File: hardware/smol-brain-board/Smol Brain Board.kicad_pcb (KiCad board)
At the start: 2 copper layers, 44.8 x 52.6 mm, 66 parts, among them J1 USB4085-GF-A, J12 Jumper 2Way Vert Solderable, J3 CAN_DBG, J6 Smol_Brain_Board, J7 PROGRAM, J8 Jumper 2Way Vert Solderable, J9 Jumper 2Way Vert Solderable, U1 ESP32-S3-WROOM-1-N8, U3 SN65HVD231D

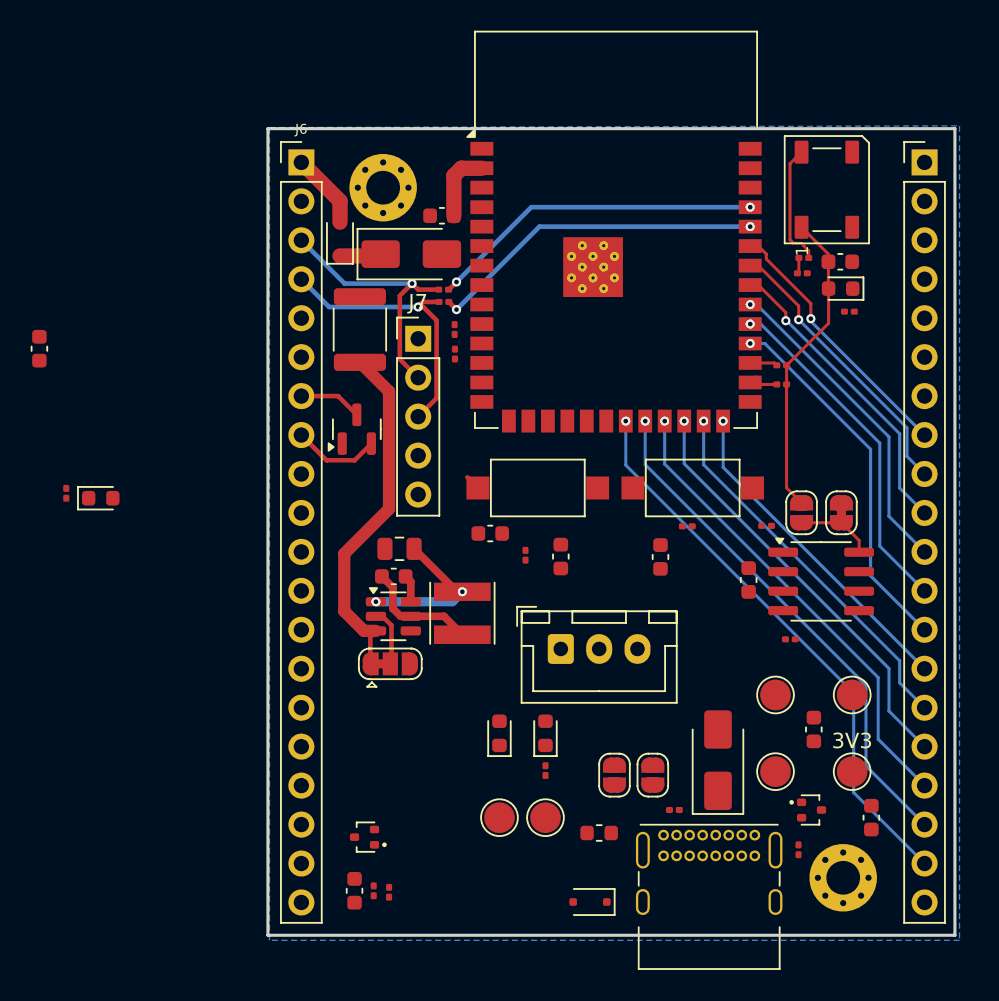
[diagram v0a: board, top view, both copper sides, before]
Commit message: Impedence matching USB data
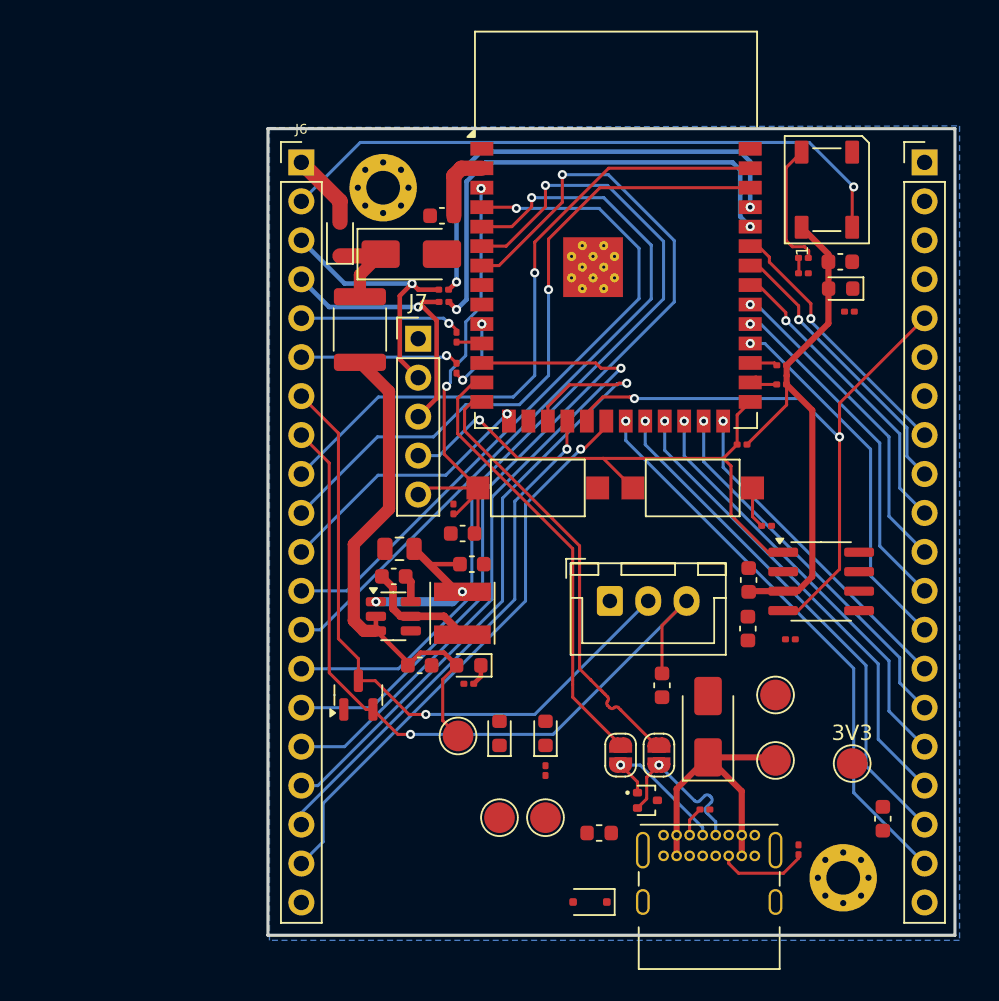
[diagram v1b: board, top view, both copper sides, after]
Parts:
- removed C12: Capacitor 100n 50V 0603, Capacitor_SMD:C_0603_1608Metric
- removed D7: RB558WMTL, Package_TO_SOT_SMD:SOT-416
- removed J12: Jumper 2Way Vert Solderable, Jumper:SolderJumper-2_P1.3mm_Open_RoundedPad1.0x1.5mm
- removed JP1: SolderJumper_2_Bridged, Jumper:SolderJumper-2_P1.3mm_Bridged_RoundedPad1.0x1.5mm
- removed JP3: SolderJumper_3_Bridged12, Jumper:SolderJumper-3_P1.3mm_Bridged12_RoundedPad1.0x1.5mm
- removed R10, R11: Resistor 10k 0603, Resistor_SMD:R_0201_0603Metric
- moved C4 32.3 mm to (135.9, 113.8), turned to 0 degrees
- moved R9 29.0 mm to (139.1, 115.0), turned to 180 degrees
- moved VIN_IND1 26.4 mm to (139.1, 113.8), turned to 180 degrees
- moved C6 24.8 mm to (139.3, 107.2), turned to 0 degrees
- moved VCC1 20.8 mm to (138.4, 118.4)
- moved D3 17.3 mm to (131.9, 115.7)
- moved D6 10.7 mm to (150.8, 122.6)
- moved C11 10.7 mm to (151.7, 115.1), turned to -90 degrees
- moved C8 7.37 mm to (157.3, 111.4)
- moved VBUS1 6.58 mm to (159.1, 120.0)
- moved R19 6.42 mm to (156.9, 99.4)
- moved R6 5.59 mm to (138.1, 103.6), turned to -90 degrees
- moved J3 4.48 mm to (148.3, 109.6)
- moved D2 2.28 mm to (154.7, 117.8)
- moved R4 1.99 mm to (154.5, 123.2), turned to 0 degrees
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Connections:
- C4 pad 1: Net-(JP3-A) -> Net-(VIN_IND1-A)
- F1 pad 1: Net-(JP3-A) -> Net-(VIN_IND1-A)
- F2 pad 2: Net-(JP3-A) -> Net-(VIN_IND1-A)
- U3 pad 8: Net-(J12-A) -> GND
- VCC1 pad 1: Net-(JP3-A) -> Net-(VIN_IND1-A)
- VIN_IND1 pad 2: Net-(JP3-A) -> Net-(VIN_IND1-A)
- VR1 pad 2: Net-(JP3-C) -> Net-(VIN_IND1-A)
- VR1 pad 3: Net-(JP3-A) -> Net-(VIN_IND1-A)
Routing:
- net /A7: track 0.00 -> 61.0 mm, vias 0 -> 1
- net /A6: track 0.00 -> 57.2 mm, vias 0 -> 1
- net /A5: track 0.00 -> 48.7 mm, vias 0 -> 1
- net /A4: track 0.00 -> 44.6 mm, vias 0 -> 1
- net /CAN_L: track 5.70 -> 50.2 mm, vias 0 -> 1
- net /A8: track 0.00 -> 44.2 mm, vias 0 -> 1
- net /A2: track 0.00 -> 43.3 mm, vias 0 -> 1
- net /A9: track 0.00 -> 42.7 mm, vias 0 -> 1
- net /A1: track 0.00 -> 42.6 mm, vias 0 -> 1
- net /CAN_RX: track 0.00 -> 42.1 mm, vias 0 -> 2
- net /LED_DOUT: track 0.00 -> 41.5 mm, vias 0 -> 1
- net /CAN_H: track 4.13 -> 43.0 mm, vias 0 -> 1
- net /CAN_TX: track 0.00 -> 37.3 mm, vias 0 -> 1
- net /IO12: track 0.00 -> 37.2 mm, vias 0 -> 1
- net Net-(VIN_IND1-A): track 0.00 -> 33.9 mm
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
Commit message: Rough route and via stitching, needs trace width correction
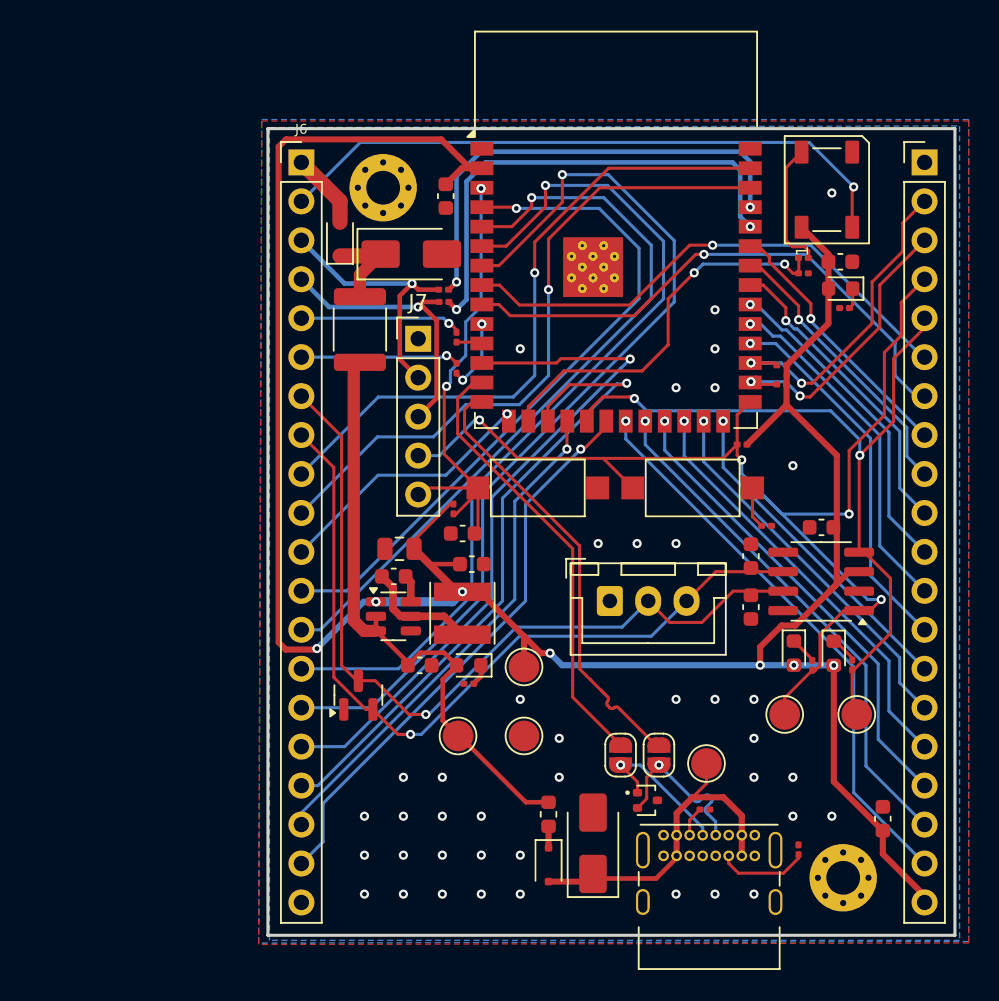
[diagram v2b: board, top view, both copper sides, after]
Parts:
- moved CAN_RX1 24.3 mm to (164.4, 117.0)
- moved 3V3 22.3 mm to (142.7, 113.9)
- moved R14 21.1 mm to (164.1, 113.8)
- moved CTX1 19.9 mm to (160.3, 113.0), turned to -90 degrees
- moved CRX1 19.5 mm to (162.9, 113.0), turned to -90 degrees
- moved CAN_TX1 17.0 mm to (159.7, 117.0)
- moved GND1 16.6 mm to (142.7, 118.4)
- moved D2 10.7 mm to (147.2, 125.4)
- moved C11 10.2 mm to (157.5, 106.7), turned to 90 degrees
- moved C7 5.86 mm to (162.1, 104.8), turned to 180 degrees
- moved VBUS1 4.50 mm to (154.6, 120.2)
- moved D4 3.63 mm to (144.3, 126.8), turned to -90 degrees
- moved F2 3.52 mm to (144.3, 123.5), turned to 90 degrees
- moved R12 2.22 mm to (161.5, 113.8), turned to 90 degrees
- moved C8 1.41 mm to (157.5, 110.0)
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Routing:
- net 3V3: track 54.1 -> 161.8 mm, vias 2 -> 7
- net /CAN_TX: track 37.3 -> 78.5 mm, vias 1 -> 4
- net /IO16: track 0.00 -> 36.6 mm, vias 0 -> 1
- net /IO15: track 0.00 -> 34.0 mm, vias 0 -> 1
- net /uC_LED: track 1.04 -> 25.4 mm, vias 0 -> 2
- net /I2C_SCK: track 1.80 -> 21.2 mm, vias 0 -> 2
- net /I2C_SDA: track 2.31 -> 19.9 mm, vias 0 -> 2
- net /CAN_H: track 43.0 -> 53.3 mm
- net /CAN_RX: track 42.1 -> 51.1 mm
- net Net-(VIN_IND1-A): track 33.9 -> 40.0 mm
- net VBUS: track 19.1 -> 22.5 mm
- net Net-(CRX1-K): track 0.00 -> 1.80 mm
- net Net-(CTX1-K): track 0.00 -> 1.76 mm
- net /CAN_L: track 50.2 -> 51.9 mm
- net /A8: track 44.2 -> 45.6 mm
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- added copper zone on F.Cu, net GND

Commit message: Routing complete, DRC passing, inspection required
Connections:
- J6 pad 41: GND -> (no net)
- J6 pad 42: GND -> (no net)
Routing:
- net GND: vias 40 -> 75

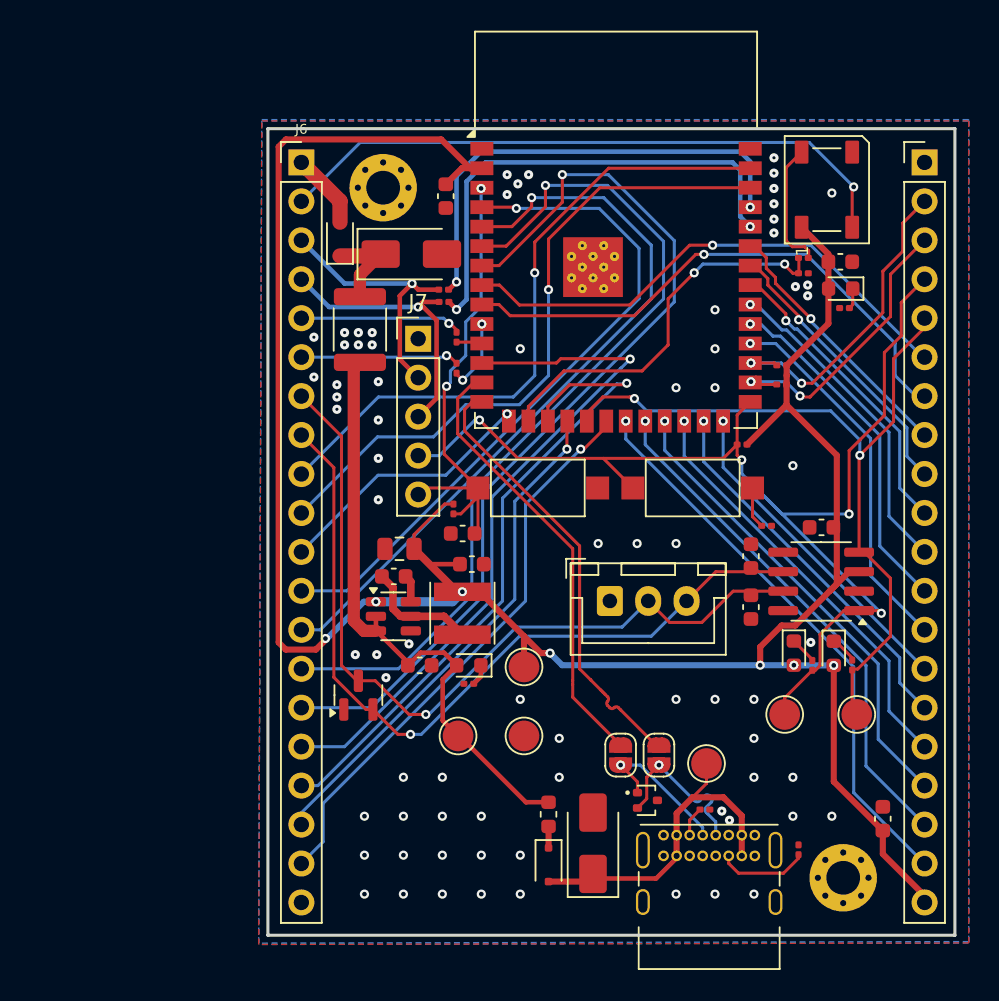
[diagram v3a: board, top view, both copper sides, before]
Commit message: Fixed impedance matching for USB and decoupling cap placement
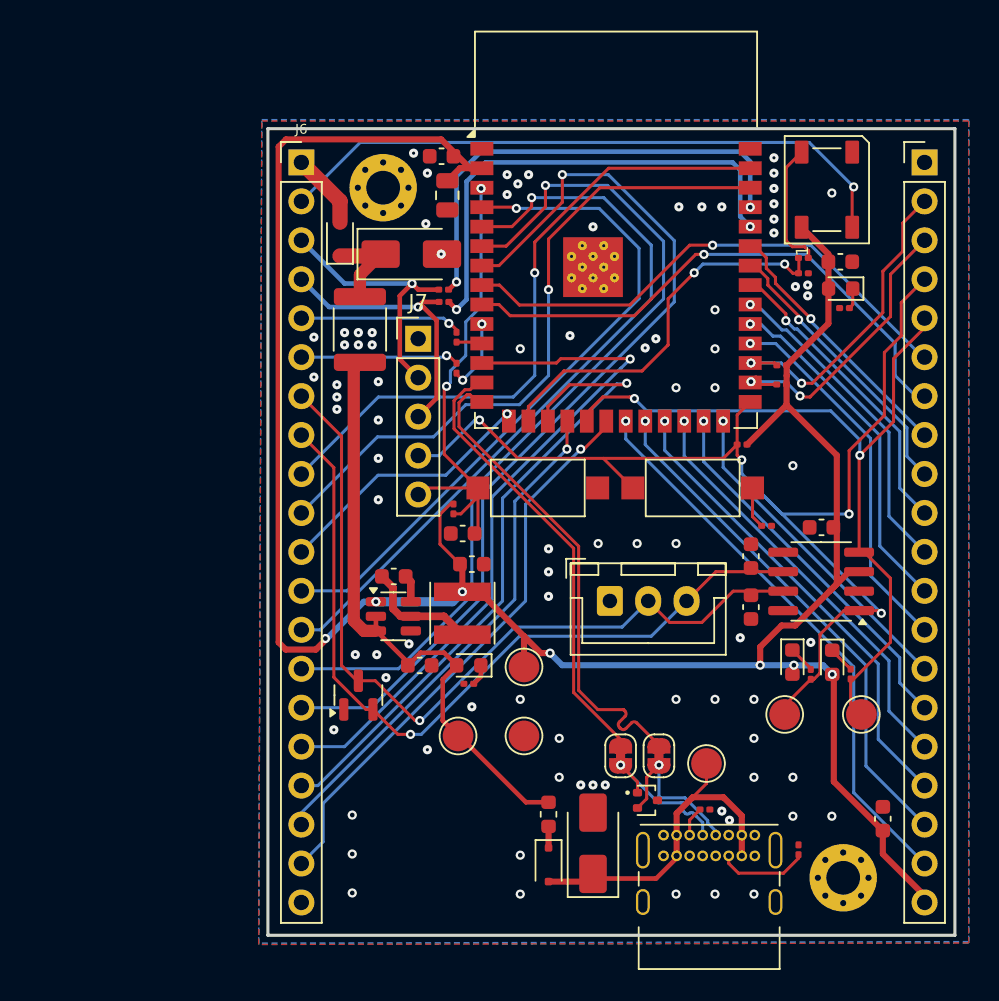
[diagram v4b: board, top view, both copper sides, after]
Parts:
- removed J8, J9: Jumper 2Way Vert Solderable, Jumper:SolderJumper-2_P1.3mm_Open_RoundedPad1.0x1.5mm
- added JP1: SolderJumper_2_Bridged, Jumper:SolderJumper-2_P1.3mm_Bridged_RoundedPad1.0x1.5mm, F.Cu at (149.0, 119.7)
- added JP2: SolderJumper_2_Bridged, Jumper:SolderJumper-2_P1.3mm_Bridged_RoundedPad1.0x1.5mm, F.Cu at (151.5, 119.7)
- moved C1 23.3 mm to (137.7, 83.2), turned to 90 degrees
- moved C2 2.61 mm to (137.3, 80.6), turned to 0 degrees
- moved CTX1 0.60 mm to (160.2, 113.6)
- moved R12 0.60 mm to (161.4, 114.4)
- moved R14 0.60 mm to (164.0, 114.4)
- moved CRX1 0.60 mm to (162.8, 113.6)
- moved CAN_RX1 0.30 mm to (164.7, 117.0)
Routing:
- net 3V3: track 162.1 -> 156.6 mm
- net /uC_USB_D_N: track 29.3 -> 33.0 mm
- net /USB_D_P: track 9.79 -> 10.4 mm
- net GND: vias 75 -> 85
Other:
- board text added: "JCN MRB"
- board text added: "Smol Brain Board v1.1"
